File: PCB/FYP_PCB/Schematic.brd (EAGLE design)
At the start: 100 x 100 mm, 14 parts, among them IC1 7805TV

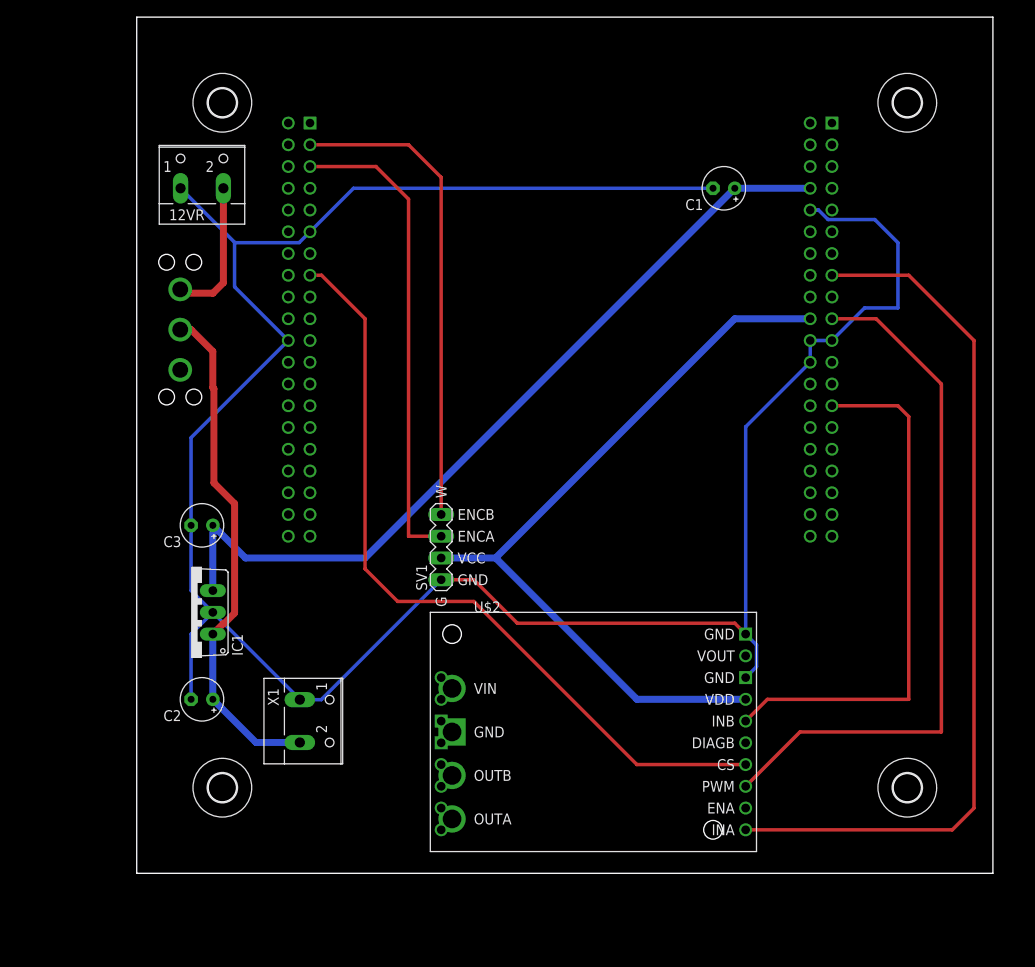
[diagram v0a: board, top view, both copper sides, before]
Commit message: Update PCB for new pin configurations. Add HC05 bluetooth module.
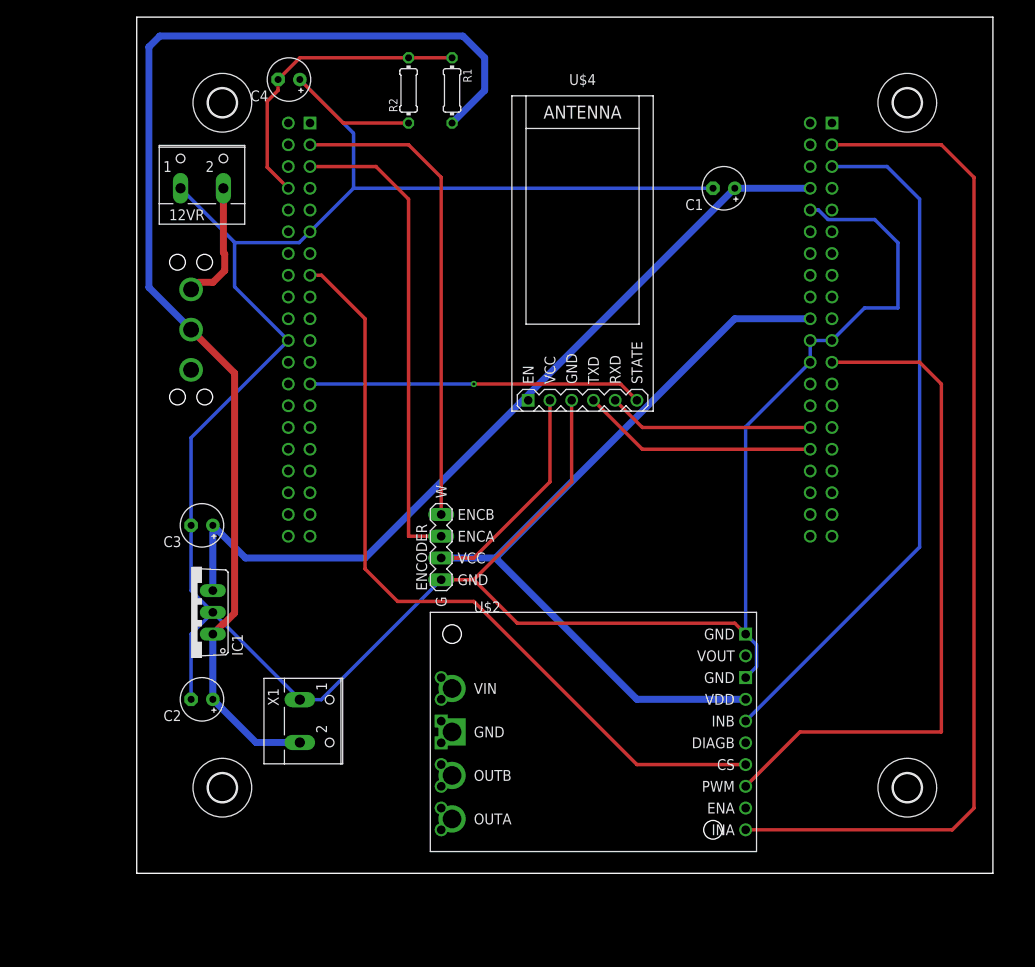
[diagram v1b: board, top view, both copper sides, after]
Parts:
- added C4: 100nF, rcl:E2,5-5
- added R1, R2: (no value), rcl:0204/7
- added U$4: WIRELESS-BLUETOOTH-HC-05, BT_6pin:WIRELESS-BLUETOOTH-HC-05
- moved U$3 1.27 mm to (6.35, 63.5)
- renumbered SV1 to ENCODER
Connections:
- new net EN(VCC): U$4.1
- new net N$11: U$1.CN7_28, U$4.5
- new net N$12: U$1.CN10_23, U$4.6
- new net N$15: C4.-, R1.1, R2.2, U$1.CN10_6
- new net N$9: U$1.CN7_30, U$4.4
- net +12V: now also R1.2
- net GND: now also C4.+, R2.1, U$4.3
- net N$1: now also U$1.CN7_1; no longer U$1.CN7_13
- net N$2: now also U$1.CN7_21; no longer U$1.CN7_17
- net N$4: now also U$1.CN7_3; no longer U$1.CN7_25
- net N$5: now also U$4.2
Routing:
- net +12V: track 59.9 -> 143.7 mm
- net GND: track 279.9 -> 335.7 mm
- net N$12: track 0.00 -> 39.0 mm, vias 0 -> 1
- net N$15: track 0.00 -> 35.6 mm
- net N$9: track 0.00 -> 27.7 mm
- net N$5: track 90.7 -> 116.6 mm
- net N$11: track 0.00 -> 24.1 mm
- net N$4: track 62.6 -> 81.2 mm
- net N$1: track 102.1 -> 119.6 mm
- net N$8: track 16.8 -> 14.5 mm
- net N$2: track 82.1 -> 80.0 mm

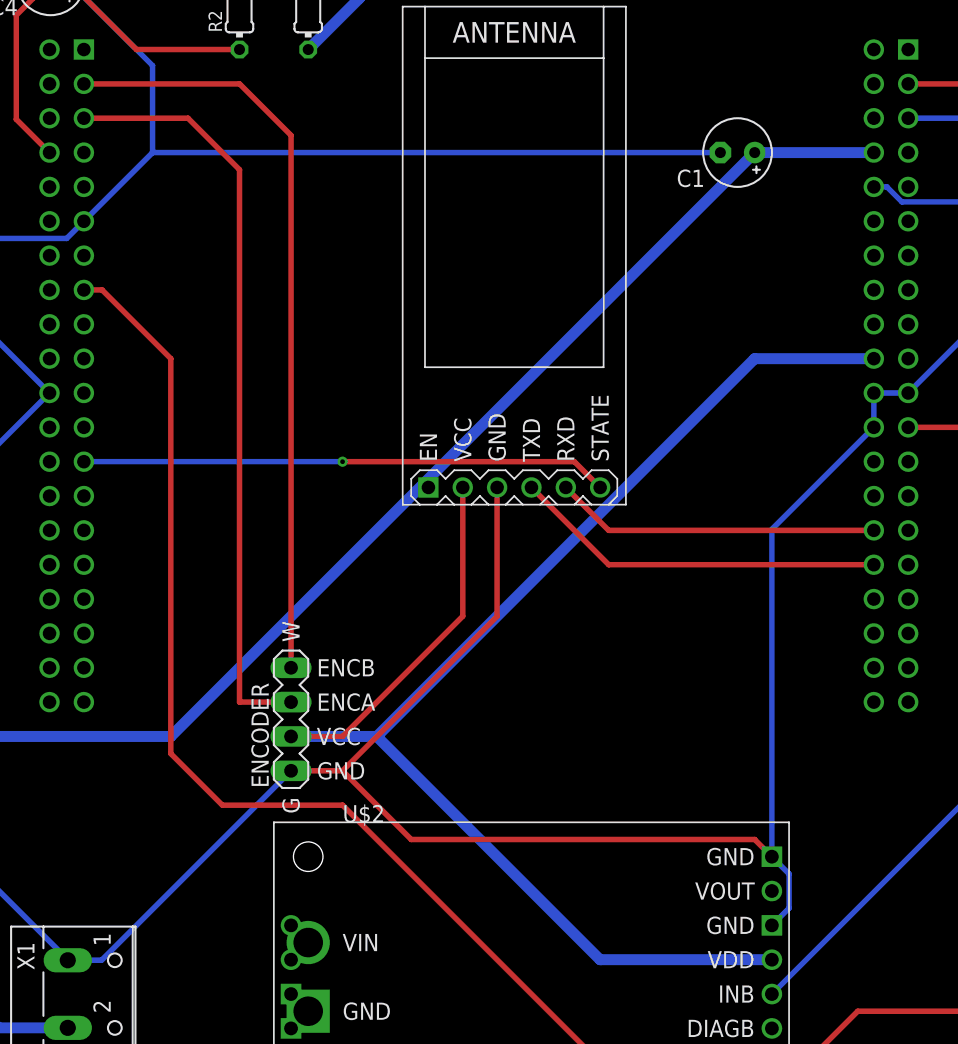
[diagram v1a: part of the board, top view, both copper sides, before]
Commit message: Eagle garbage I cant gitignore.
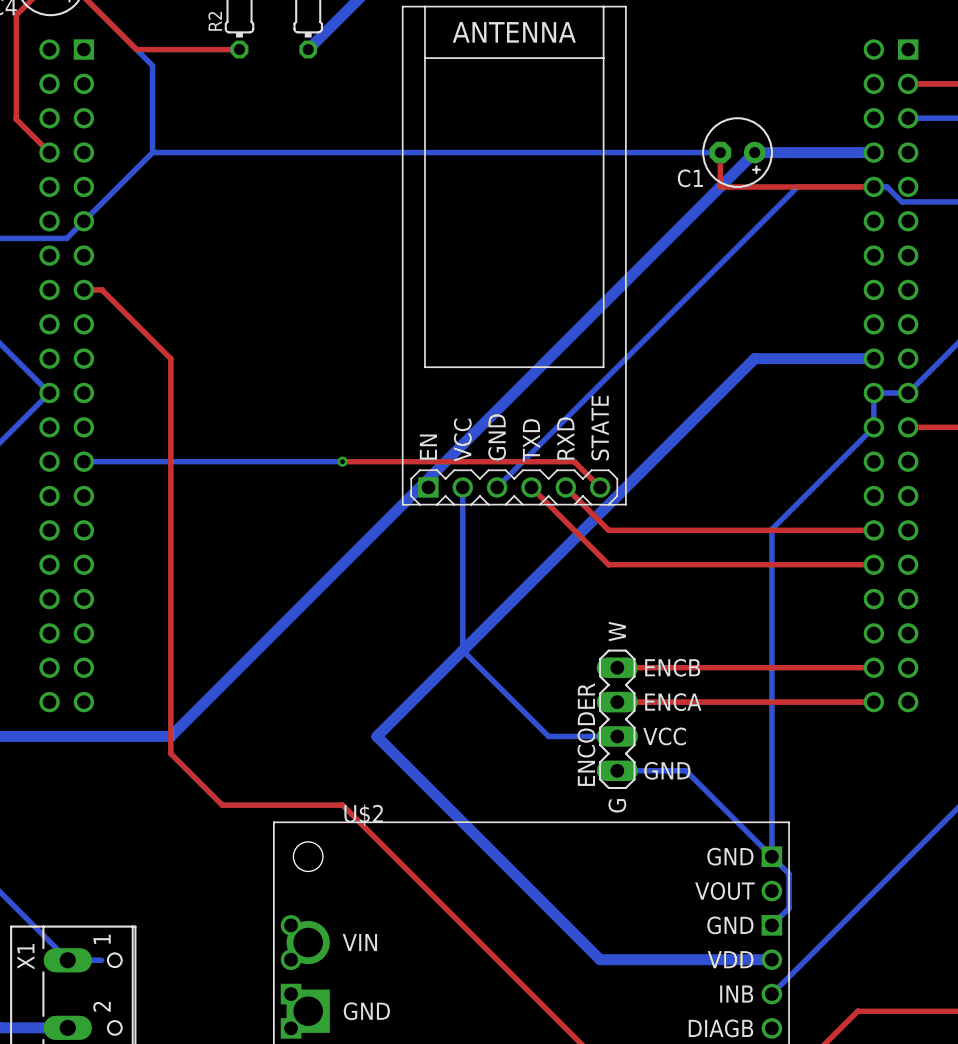
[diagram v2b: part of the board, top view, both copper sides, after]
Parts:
- R1: value (none) -> 30k
- R2: value (none) -> 5.1k
- moved ENCODER 24.1 mm to (59.7, 38.1)
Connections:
- net N$6: now also U$1.CN7_36; no longer U$1.CN10_1
- net N$7: now also U$1.CN7_38; no longer U$1.CN10_3
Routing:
- net N$6: track 56.3 -> 19.0 mm
- net N$7: track 56.3 -> 19.0 mm
- net GND: track 335.7 -> 317.0 mm
- net N$5: track 116.6 -> 111.8 mm
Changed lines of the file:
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@@
 <attribute name="VALUE" x="40.005" y="1.27" size="1.27" layer="27"/>
 </element>
-<element name="ENCODER" library="Custom" package="MA04-1" package3d_urn="urn:adsk.eagle:package:8337/1" value="" x="35.56" y="38.1" smashed="yes" rot="R90">
-<attribute name="MF" value="" x="35.56" y="38.1" size="1.778" layer="27" rot="R90" display="off"/>
-<attribute name="MPN" value="" x="35.56" y="38.1" size="1.778" layer="27" rot="R90" display="off"/>
-<attribute name="NAME" x="33.909" y="33.02" size="1.27" layer="25" ratio="10" rot="R90"/>
-<attribute name="OC_FARNELL" value="unknown" x="35.56" y="38.1" size="1.778" layer="27" rot="R90" display="off"/>
-<attribute name="OC_NEWARK" value="unknown" x="35.56" y="38.1" size="1.778" layer="27" rot="R90" display="off"/>
-<attribute name="POPULARITY" value="41" x="35.56" y="38.1" size="1.778" layer="27" rot="R90" display="off"/>
-<attribute name="VALUE" x="33.909" y="38.735" size="1.27" layer="27" ratio="10" rot="R90"/>
+<element name="ENCODER" library="Custom" package="MA04-1" package3d_urn="urn:adsk.eagle:package:8337/1" value="" x="59.69" y="38.1" smashed="yes" rot="R90">
+<attribute name="MF" value="" x="59.69" y="38.1" size="1.778" layer="27" rot="R90" display="off"/>
+<attribute name="MPN" value="" x="59.69" y="38.1" size="1.778" layer="27" rot="R90" display="off"/>
+<attribute name="NAME" x="58.039" y="33.02" size="1.27" layer="25" ratio="10" rot="R90"/>
+<attribute name="OC_FARNELL" value="unknown" x="59.69" y="38.1" size="1.778" layer="27" rot="R90" display="off"/>
+<attribute name="OC_NEWARK" value="unknown" x="59.69" y="38.1" size="1.778" layer="27" rot="R90" display="off"/>
+<attribute name="POPULARITY" value="41" x="59.69" y="38.1" size="1.778" layer="27" rot="R90" display="off"/>
+<attribute name="VALUE" x="58.039" y="38.735" size="1.27" layer="27" ratio="10" rot="R90"/>
 </element>
 <element name="X1" library="con-wago-500" library_urn="urn:adsk.eagle:library:195" package="W237-102" package3d_urn="urn:adsk.eagle:package:10688/1" value="" x="20.32" y="17.78" smashed="yes" rot="R270">
@@
 <attribute name="VALUE" x="52.07" y="52.705" size="1.27" layer="27" align="top-center"/>
 </element>
-<element name="R1" library="rcl" library_urn="urn:adsk.eagle:library:334" package="0204/7" package3d_urn="urn:adsk.eagle:package:23498/2" value="" x="36.83" y="91.44" smashed="yes" rot="R270">
+<element name="R1" library="rcl" library_urn="urn:adsk.eagle:library:334" package="0204/7" package3d_urn="urn:adsk.eagle:package:23498/2" value="30k" x="36.83" y="91.44" smashed="yes" rot="R270">
 <attribute name="NAME" x="38.1254" y="93.98" size="0.9906" layer="25" ratio="10" rot="R270"/>
 <attribute name="POPULARITY" value="48" x="36.83" y="91.44" size="1.778" layer="27" rot="R270" display="off"/>
@@
 <attribute name="VALUE" x="36.3474" y="93.0656" size="0.9906" layer="27" ratio="10" rot="R270"/>
 </element>
-<element name="R2" library="rcl" library_urn="urn:adsk.eagle:library:334" package="0204/7" package3d_urn="urn:adsk.eagle:package:23498/2" value="" x="31.75" y="91.44" smashed="yes" rot="R90">
+<element name="R2" library="rcl" library_urn="urn:adsk.eagle:library:334" package="0204/7" package3d_urn="urn:adsk.eagle:package:23498/2" value="5.1k" x="31.75" y="91.44" smashed="yes" rot="R90">
 <attribute name="NAME" x="30.4546" y="88.9" size="0.9906" layer="25" ratio="10" rot="R90"/>
 <attribute name="POPULARITY" value="48" x="31.75" y="91.44" size="1.778" layer="27" rot="R90" display="off"/>
@@
 <contactref element="U$2" pad="VDD"/>
 <contactref element="U$1" pad="CN7_18"/>
-<contactref element="ENCODER" pad="VCC"/>
 <wire x1="71.12" y1="20.32" x2="58.42" y2="20.32" width="0.8128" layer="16"/>
-<wire x1="41.91" y1="36.83" x2="35.56" y2="36.83" width="0.8128" layer="16"/>
 <wire x1="58.42" y1="20.32" x2="41.91" y2="36.83" width="0.8128" layer="16"/>
-<wire x1="69.85" y1="64.77" x2="41.91" y2="36.83" width="0.8128" layer="16"/>
+<wire x1="69.85" y1="64.77" x2="48.26" y2="43.18" width="0.8128" layer="16"/>
+<wire x1="48.26" y1="43.18" x2="41.91" y2="36.83" width="0.8128" layer="16"/>
 <wire x1="78.66" y1="64.77" x2="69.85" y2="64.77" width="0.8128" layer="16"/>
 <contactref element="U$4" pad="2"/>
-<wire x1="35.56" y1="36.83" x2="39.37" y2="36.83" width="0.4064" layer="1"/>
-<wire x1="39.37" y1="36.83" x2="48.26" y2="45.72" width="0.4064" layer="1"/>
-<wire x1="48.26" y1="45.72" x2="48.26" y2="55.245" width="0.4064" layer="1"/>
+<contactref element="ENCODER" pad="VCC"/>
+<wire x1="58.42" y1="36.83" x2="59.69" y2="36.83" width="0.4064" layer="1"/>
+<wire x1="48.26" y1="55.245" x2="48.26" y2="43.18" width="0.4064" layer="16"/>
+<wire x1="59.69" y1="36.83" x2="54.61" y2="36.83" width="0.4064" layer="16"/>
+<wire x1="54.61" y1="36.83" x2="48.26" y2="43.18" width="0.4064" layer="16"/>
 </signal>
 <signal name="GND">
@@
 <contactref element="U$1" pad="CN7_8"/>
 <contactref element="U$1" pad="CN10_9"/>
-<contactref element="ENCODER" pad="GND"/>
 <contactref element="U$1" pad="CN10_20"/>
 <contactref element="U$1" pad="CN7_19"/>
@@
 <wire x1="11.43" y1="73.66" x2="11.43" y2="68.5" width="0.4064" layer="16"/>
 <wire x1="11.43" y1="68.5" x2="17.7" y2="62.23" width="0.4064" layer="16"/>
-<wire x1="35.56" y1="34.29" x2="21.55" y2="20.28" width="0.4064" layer="16"/>
 <wire x1="21.55" y1="20.28" x2="19.05" y2="20.28" width="0.4064" layer="16"/>
 <wire x1="6.35" y1="40.64" x2="6.35" y2="33.02" width="0.4064" layer="16"/>
 <wire x1="6.35" y1="33.02" x2="8.89" y2="30.48" width="0.4064" layer="16"/>
-<wire x1="71.12" y1="27.94" x2="69.85" y2="29.21" width="0.4064" layer="1"/>
-<wire x1="69.85" y1="29.21" x2="44.45" y2="29.21" width="0.4064" layer="1"/>
-<wire x1="44.45" y1="29.21" x2="39.37" y2="34.29" width="0.4064" layer="1"/>
-<wire x1="39.37" y1="34.29" x2="35.56" y2="34.29" width="0.4064" layer="1"/>
 <wire x1="20.24" y1="74.93" x2="25.32" y2="80.01" width="0.4064" layer="16"/>
 <wire x1="25.32" y1="80.01" x2="67.31" y2="80.01" width="0.4064" layer="16"/>
@@
 <wire x1="11.43" y1="73.7" x2="11.43" y2="73.66" width="0.4064" layer="16"/>
 <contactref element="U$4" pad="3"/>
-<wire x1="50.8" y1="55.245" x2="50.8" y2="45.72" width="0.4064" layer="1"/>
-<wire x1="50.8" y1="45.72" x2="39.37" y2="34.29" width="0.4064" layer="1"/>
 <contactref element="R2" pad="1"/>
 <contactref element="C4" pad="+"/>
@@
 <wire x1="31.75" y1="87.63" x2="24.13" y2="87.63" width="0.4064" layer="1"/>
 <wire x1="24.13" y1="87.63" x2="19.05" y2="92.71" width="0.4064" layer="1"/>
+<contactref element="ENCODER" pad="GND"/>
+<wire x1="59.69" y1="34.29" x2="64.77" y2="34.29" width="0.4064" layer="16"/>
+<wire x1="64.77" y1="34.29" x2="71.12" y2="27.94" width="0.4064" layer="16"/>
+<wire x1="50.8" y1="55.245" x2="73.025" y2="77.47" width="0.4064" layer="16"/>
+<wire x1="73.025" y1="77.47" x2="78.66" y2="77.47" width="0.4064" layer="16"/>
+<wire x1="67.31" y1="80.01" x2="67.31" y2="77.47" width="0.4064" layer="1"/>
+<wire x1="67.31" y1="77.47" x2="78.66" y2="77.47" width="0.4064" layer="1"/>
 </signal>
 <signal name="+12V">
@@
 <wire x1="12.7" y1="36.83" x2="8.89" y2="40.64" width="0.8128" layer="16"/>
 </signal>
-<signal name="N$6">
-<contactref element="ENCODER" pad="ENCB"/>
-<contactref element="U$1" pad="CN10_1"/>
-<wire x1="35.56" y1="41.91" x2="35.56" y2="81.28" width="0.4064" layer="1"/>
-<wire x1="35.56" y1="81.28" x2="31.75" y2="85.09" width="0.4064" layer="1"/>
-<wire x1="31.75" y1="85.09" x2="20.24" y2="85.09" width="0.4064" layer="1"/>
-</signal>
-<signal name="N$7">
-<contactref element="ENCODER" pad="ENCA"/>
-<contactref element="U$1" pad="CN10_3"/>
-<wire x1="35.56" y1="39.37" x2="31.75" y2="39.37" width="0.4064" layer="1"/>
-<wire x1="31.75" y1="39.37" x2="31.75" y2="78.74" width="0.4064" layer="1"/>
-<wire x1="31.75" y1="78.74" x2="27.94" y2="82.55" width="0.4064" layer="1"/>
-<wire x1="27.94" y1="82.55" x2="20.24" y2="82.55" width="0.4064" layer="1"/>
-</signal>
 <signal name="N$8">
 <contactref element="U$3" pad="1"/>
@@
 <wire x1="31.75" y1="95.25" x2="36.83" y2="95.25" width="0.4064" layer="1"/>
 </signal>
+<signal name="N$6">
+<contactref element="U$1" pad="CN7_36"/>
+<contactref element="ENCODER" pad="ENCB"/>
+<wire x1="59.69" y1="41.91" x2="78.66" y2="41.91" width="0.4064" layer="1"/>
+</signal>
+<signal name="N$7">
+<contactref element="U$1" pad="CN7_38"/>
+<contactref element="ENCODER" pad="ENCA"/>
+<wire x1="59.69" y1="39.37" x2="78.66" y2="39.37" width="0.4064" layer="1"/>
+</signal>
 </signals>
